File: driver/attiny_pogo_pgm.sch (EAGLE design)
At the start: 9 parts, among them IC1 ATTiny85, J1 AVR_SPI_PRG_6NS, P5V TPTP10R

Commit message: prepare for routing
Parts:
- removed IC1: ATTiny85, atmel:TINY13-20SU
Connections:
- net +5V: no longer IC1.VCC
- net GND: no longer IC1.GND
- net IN1/MISO: no longer IC1.PB1/PCINT1/AIN1/OC0B/INT0/MISO
- net RESET-: no longer IC1.PB5/PCINT5/!RESET!/ADC0/DW
- net SCL/SCK: no longer IC1.PB2/PCINT2/SCK/ADC1/T0
- net SDA/MOSI: no longer IC1.PB0/PCINT0/AIN0/OC0A/MOSI
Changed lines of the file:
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@@
 </classes>
 <parts>
-<part name="IC1" library="atmel" deviceset="TINY13" device="SU" technology="-20" value="ATTiny85"/>
 <part name="GND3" library="supply1" deviceset="GND" device=""/>
 <part name="P+4" library="supply1" deviceset="+5V" device=""/>
@@
 </plain>
 <instances>
-<instance part="IC1" gate="G$1" x="30.48" y="78.74" rot="R180"/>
 <instance part="GND3" gate="1" x="50.8" y="86.36" rot="R180"/>
 <instance part="P+4" gate="1" x="50.8" y="63.5" rot="R180"/>
@@
 <net name="IN1/MISO" class="0">
 <segment>
-<pinref part="IC1" gate="G$1" pin="PB1/PCINT1/AIN1/OC0B/INT0/MISO"/>
 <wire x1="50.8" y1="71.12" x2="53.34" y2="71.12" width="0.1524" layer="91"/>
 <pinref part="J1" gate="G$1" pin="1"/>
@@
 </net>
 <net name="GND" class="0">
-<segment>
-<pinref part="IC1" gate="G$1" pin="GND"/>
-<pinref part="GND3" gate="1" pin="GND"/>
-</segment>
 <segment>
 <pinref part="J1" gate="G$1" pin="6"/>
@@
 <net name="+5V" class="0">
 <segment>
-<pinref part="IC1" gate="G$1" pin="VCC"/>
-<pinref part="P+4" gate="1" pin="+5V"/>
-</segment>
-<segment>
 <pinref part="J1" gate="G$1" pin="2"/>
 <pinref part="P+5" gate="1" pin="+5V"/>
@@
 <net name="SDA/MOSI" class="0">
 <segment>
-<pinref part="IC1" gate="G$1" pin="PB0/PCINT0/AIN0/OC0A/MOSI"/>
 <wire x1="50.8" y1="68.58" x2="83.82" y2="68.58" width="0.1524" layer="91"/>
 <wire x1="83.82" y1="68.58" x2="83.82" y2="93.98" width="0.1524" layer="91"/>
@@
 <net name="RESET-" class="0">
 <segment>
-<pinref part="IC1" gate="G$1" pin="PB5/PCINT5/!RESET!/ADC0/DW"/>
 <pinref part="J1" gate="G$1" pin="5"/>
 <wire x1="50.8" y1="81.28" x2="58.42" y2="81.28" width="0.1524" layer="91"/>
@@
 <net name="SCL/SCK" class="0">
 <segment>
-<pinref part="IC1" gate="G$1" pin="PB2/PCINT2/SCK/ADC1/T0"/>
 <wire x1="50.8" y1="73.66" x2="55.88" y2="73.66" width="0.1524" layer="91"/>
 <pinref part="J1" gate="G$1" pin="3"/>

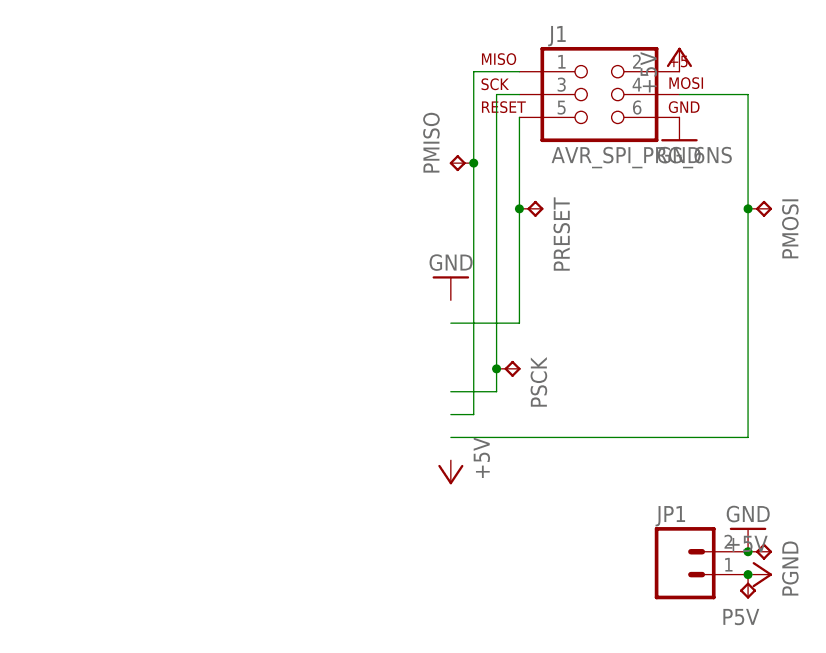
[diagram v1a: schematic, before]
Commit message: use slightly bigger pads for the pogo pins
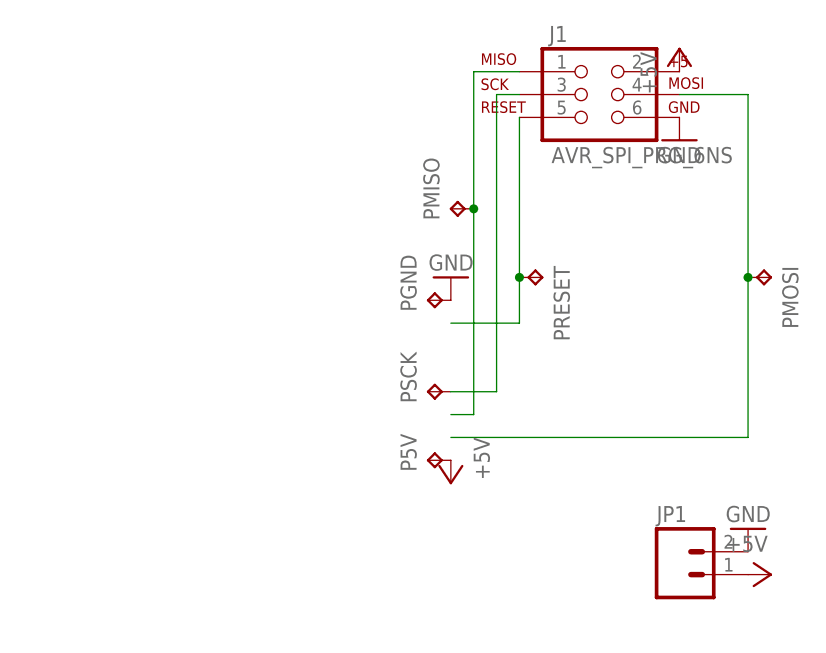
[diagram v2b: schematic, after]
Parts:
- P5V, PGND, PMISO, PMOSI, PRESET, PSCK: value TPTP10R -> TPTP12R; device testpad:TPTP10R -> testpad:TPTP12R
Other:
- moved on the sheet: P5V, PGND, PMISO, PMOSI, PRESET, PSCK
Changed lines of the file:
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@@
 <part name="P+1" library="supply1" deviceset="+5V" device=""/>
 <part name="GND1" library="supply1" deviceset="GND" device=""/>
-<part name="PMOSI" library="testpad" deviceset="TP" device="TP10R"/>
-<part name="PRESET" library="testpad" deviceset="TP" device="TP10R"/>
-<part name="PSCK" library="testpad" deviceset="TP" device="TP10R">
-<attribute name="TP_SIGNAL_NAME" value=""/>
-</part>
-<part name="PMISO" library="testpad" deviceset="TP" device="TP10R">
-<attribute name="TP_SIGNAL_NAME" value=""/>
-</part>
-<part name="PGND" library="testpad" deviceset="TP" device="TP10R">
-<attribute name="TP_SIGNAL_NAME" value=""/>
-</part>
-<part name="P5V" library="testpad" deviceset="TP" device="TP10R">
-<attribute name="TP_SIGNAL_NAME" value=""/>
-</part>
+<part name="PMOSI" library="testpad" deviceset="TP" device="TP12R"/>
+<part name="PMISO" library="testpad" deviceset="TP" device="TP12R"/>
+<part name="PSCK" library="testpad" deviceset="TP" device="TP12R"/>
+<part name="PRESET" library="testpad" deviceset="TP" device="TP12R"/>
+<part name="PGND" library="testpad" deviceset="TP" device="TP12R"/>
+<part name="P5V" library="testpad" deviceset="TP" device="TP12R"/>
 </parts>
 <sheets>
@@
 <instance part="P+1" gate="1" x="86.36" y="53.34" rot="R270"/>
 <instance part="GND1" gate="1" x="83.82" y="58.42" rot="R180"/>
-<instance part="PMOSI" gate="G$1" x="86.36" y="93.98" rot="R270"/>
-<instance part="PRESET" gate="G$1" x="60.96" y="93.98" rot="R270"/>
-<instance part="PSCK" gate="G$1" x="58.42" y="76.2" rot="R270"/>
-<instance part="PMISO" gate="G$1" x="50.8" y="99.06" rot="R90"/>
-<instance part="PGND" gate="G$1" x="86.36" y="55.88" rot="R270"/>
-<instance part="P5V" gate="G$1" x="83.82" y="50.8" rot="R180"/>
+<instance part="PMOSI" gate="G$1" x="86.36" y="86.36" rot="R270"/>
+<instance part="PMISO" gate="G$1" x="50.8" y="93.98" rot="R90"/>
+<instance part="PSCK" gate="G$1" x="48.26" y="73.66" rot="R90"/>
+<instance part="PRESET" gate="G$1" x="60.96" y="86.36" rot="R270"/>
+<instance part="PGND" gate="G$1" x="48.26" y="83.82" rot="R90"/>
+<instance part="P5V" gate="G$1" x="48.26" y="66.04" rot="R90"/>
 </instances>
 <busses>
@@
 <pinref part="J1" gate="G$1" pin="1"/>
 <wire x1="58.42" y1="109.22" x2="53.34" y2="109.22" width="0.1524" layer="91"/>
-<wire x1="53.34" y1="109.22" x2="53.34" y2="99.06" width="0.1524" layer="91"/>
+<wire x1="53.34" y1="109.22" x2="53.34" y2="93.98" width="0.1524" layer="91"/>
 <pinref part="PMISO" gate="G$1" pin="TP"/>
-<wire x1="53.34" y1="99.06" x2="53.34" y2="71.12" width="0.1524" layer="91"/>
-<junction x="53.34" y="99.06"/>
+<wire x1="53.34" y1="93.98" x2="53.34" y2="71.12" width="0.1524" layer="91"/>
+<junction x="53.34" y="93.98"/>
 </segment>
 </net>
@@
 <pinref part="JP1" gate="G$1" pin="2"/>
 <pinref part="GND1" gate="1" pin="GND"/>
-<junction x="83.82" y="55.88"/>
+</segment>
+<segment>
+<pinref part="GND3" gate="1" pin="GND"/>
 <pinref part="PGND" gate="G$1" pin="TP"/>
 </segment>
@@
 <pinref part="JP1" gate="G$1" pin="1"/>
 <pinref part="P+1" gate="1" pin="+5V"/>
-<junction x="83.82" y="53.34"/>
+</segment>
+<segment>
+<pinref part="P+4" gate="1" pin="+5V"/>
 <pinref part="P5V" gate="G$1" pin="TP"/>
 </segment>
@@
 <segment>
 <wire x1="50.8" y1="68.58" x2="83.82" y2="68.58" width="0.1524" layer="91"/>
-<wire x1="83.82" y1="68.58" x2="83.82" y2="93.98" width="0.1524" layer="91"/>
+<wire x1="83.82" y1="68.58" x2="83.82" y2="86.36" width="0.1524" layer="91"/>
 <pinref part="J1" gate="G$1" pin="4"/>
-<wire x1="83.82" y1="93.98" x2="83.82" y2="106.68" width="0.1524" layer="91"/>
+<wire x1="83.82" y1="86.36" x2="83.82" y2="106.68" width="0.1524" layer="91"/>
 <wire x1="83.82" y1="106.68" x2="76.2" y2="106.68" width="0.1524" layer="91"/>
 <pinref part="PMOSI" gate="G$1" pin="TP"/>
-<junction x="83.82" y="93.98"/>
+<junction x="83.82" y="86.36"/>
 </segment>
 </net>
@@
 <pinref part="J1" gate="G$1" pin="5"/>
 <wire x1="50.8" y1="81.28" x2="58.42" y2="81.28" width="0.1524" layer="91"/>
-<wire x1="58.42" y1="81.28" x2="58.42" y2="93.98" width="0.1524" layer="91"/>
+<wire x1="58.42" y1="81.28" x2="58.42" y2="86.36" width="0.1524" layer="91"/>
+<wire x1="58.42" y1="86.36" x2="58.42" y2="104.14" width="0.1524" layer="91"/>
 <pinref part="PRESET" gate="G$1" pin="TP"/>
-<wire x1="58.42" y1="93.98" x2="58.42" y2="104.14" width="0.1524" layer="91"/>
-<junction x="58.42" y="93.98"/>
+<junction x="58.42" y="86.36"/>
 </segment>
 </net>
@@
 <wire x1="50.8" y1="73.66" x2="55.88" y2="73.66" width="0.1524" layer="91"/>
 <pinref part="J1" gate="G$1" pin="3"/>
-<wire x1="55.88" y1="73.66" x2="55.88" y2="76.2" width="0.1524" layer="91"/>
-<wire x1="55.88" y1="76.2" x2="55.88" y2="106.68" width="0.1524" layer="91"/>
+<wire x1="55.88" y1="73.66" x2="55.88" y2="106.68" width="0.1524" layer="91"/>
 <wire x1="55.88" y1="106.68" x2="58.42" y2="106.68" width="0.1524" layer="91"/>
 <pinref part="PSCK" gate="G$1" pin="TP"/>
-<junction x="55.88" y="76.2"/>
 </segment>
 </net>
